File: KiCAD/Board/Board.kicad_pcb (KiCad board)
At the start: 2 copper layers, 84 parts, among them J1 MOTOR_5PIN_CONNECTOR, J2 DELAY_2PIN_CONNECTOR, J3 BATTERY_2PIN_CONNECTOR, Q1 AO3400A, Q2 AO3400A, Q3 AO3400A, Q4 AO3400A, Q5 SFH309, Q6 SFH309, U1 4040, U2 7421, U3 74LS393, U4 74HC164, U5 NE556, U6 ULN2003, U7 ULN2003, U8 LM7805_TO220

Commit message: Updated On May 29th 2025
KiCAD Board Almost Done. Will require minor touch ups tomm.
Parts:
- removed J2: DELAY_2PIN_CONNECTOR, Connector_PinSocket_2.54mm:PinSocket_1x02_P2.54mm_Vertical
- removed R6: R4.7K, Resistor_SMD:R_1210_3225Metric
- added C1: C0.1uf, Capacitor_THT:C_Disc_D5.0mm_W2.5mm_P2.50mm, F.Cu at (122.2, 151.6)
- added C2: C0.1uf, Capacitor_THT:C_Disc_D5.0mm_W2.5mm_P2.50mm, F.Cu at (126.5, 132.8)
- added D14: LED, LED_THT:LED_D3.0mm, F.Cu at (117.6, 69.3)
- added D15: LED, LED_THT:LED_D3.0mm, F.Cu at (112.4, 69.2)
- added D16: LED, LED_THT:LED_D3.0mm, F.Cu at (107.4, 69.2)
- added D17: LED, LED_THT:LED_D3.0mm, F.Cu at (102.4, 69.2)
- added JP1: JMP, Library:Jumper, F.Cu at (78.0, 102.1)
- added JP10: JMP, Library:Jumper, F.Cu at (58.9, 112.3)
- added JP11: JMP, Library:Jumper, F.Cu at (58.9, 114.9)
- added JP12: JMP, Library:Jumper, F.Cu at (58.9, 117.5)
- added JP13: JMP, Library:Jumper, F.Cu at (56.6, 131.3)
- added JP14: JMP, Library:Jumper, F.Cu at (15.0, 95.4)
- added JP15: JMP, Library:Jumper, F.Cu at (60.7, 122.2)
- added JP16: JMP, Library:Jumper, F.Cu at (104.9, 161.7)
- added JP17: JMP, Library:Jumper, F.Cu at (104.9, 164.3)
- added JP18: JMP, Library:Jumper, F.Cu at (84.1, 162.8)
- added JP19: JMP, Library:Jumper, F.Cu at (94.7, 122.7)
- added JP2: JMP, Library:Jumper, F.Cu at (86.9, 89.4)
- added JP20: JMP, Library:Jumper, F.Cu at (66.7, 127.4)
- added JP21: JMP, Library:Jumper, F.Cu at (136.8, 118.7)
- added JP23: JMP, Library:Jumper, F.Cu at (14.9, 106.4)
- added JP3: JMP, Library:Jumper, F.Cu at (43.9, 72.4)
- added JP4: JMP, Library:Jumper, F.Cu at (112.0, 123.7)
- added JP5: JMP, Library:Jumper, F.Cu at (85.6, 74.2)
- added JP6: JMP, Library:Jumper, F.Cu at (106.6, 113.5)
- added JP7: JMP, Library:Jumper, F.Cu at (108.5, 57.7)
- added JP8: JMP, Library:Jumper, F.Cu at (25.4, 146.1)
- added JP9: JMP, Library:Jumper, F.Cu at (34.5, 128.8)
- added R1: R4.7K, Resistor_THT:R_Axial_DIN0207_L6.3mm_D2.5mm_P10.16mm_Horizontal, F.Cu at (75.1, 96.5)
- added R2: R4.7K, Resistor_THT:R_Axial_DIN0207_L6.3mm_D2.5mm_P10.16mm_Horizontal, F.Cu at (30.7, 125.2)
- added SMD_2_DIP1: ~, Library:SMD_2_DIP, F.Cu at (85.9, 109.1)
- added SMD_2_DIP2: ~, Library:SMD_2_DIP, F.Cu at (80.8, 120.4)
- added SMD_2_DIP3: ~, Library:SMD_2_DIP, F.Cu at (50.5, 148.8)
- added SMD_2_DIP4: ~, Library:SMD_2_DIP, F.Cu at (62.7, 156.2)
- added U9: NE555P, Package_DIP:DIP-8_W7.62mm, F.Cu at (114.3, 138.2)
- C10, C13, C15, C16, C19, C23, C3, C6, C8: footprint Capacitor_SMD:C_1210_3225Metric_Pad1.33x2.70mm_HandSolder -> Capacitor_THT:C_Radial_D6.3mm_H5.0mm_P2.50mm
- C11, C12, C14, C18, C20, C21, C4, C5, C7, C9: footprint Capacitor_SMD:C_1210_3225Metric_Pad1.33x2.70mm_HandSolder -> Capacitor_THT:C_Disc_D5.0mm_W2.5mm_P2.50mm
- C17: value C0.1uf -> C10uf; footprint Capacitor_SMD:C_1210_3225Metric_Pad1.33x2.70mm_HandSolder -> Capacitor_THT:C_Radial_D6.3mm_H5.0mm_P2.50mm
- D10, D11, D12, D3, D4, D5, D6, D7, D8, D9: footprint Diode_SMD:D_1210_3225Metric -> Diode_THT:D_DO-35_SOD27_P12.70mm_Horizontal
- D2: footprint LED_SMD:LED_1210_3225Metric -> LED_THT:LED_D3.0mm
- J1: footprint Connector_PinSocket_1.27mm:PinSocket_1x05_P1.27mm_Vertical -> Connector_PinSocket_2.54mm:PinSocket_1x05_P2.54mm_Vertical
- R10, R11, R12, R13, R14, R15, R16, R17, R18, R19, R20, R21, R22, R23, R24, R25, R26, R27, R28, R29, R3, R30, R31, R32, R4, R5, R7, R8, R9: footprint Resistor_SMD:R_1210_3225Metric -> Resistor_THT:R_Axial_DIN0207_L6.3mm_D2.5mm_P10.16mm_Horizontal
- U5: value NE556 -> NE555P; footprint Package_DIP:DIP-14_W7.62mm_Socket -> Package_DIP:DIP-8_W7.62mm
- moved R4 225.8 mm to (109.5, 117.3), turned to -90 degrees
- moved R28 223.6 mm to (139.7, 86.4), turned to -90 degrees
- moved R13 223.6 mm to (127.4, 75.1), turned to 90 degrees
- moved U3 223.4 mm to (123.7, 78.0)
- moved R27 220.3 mm to (135.1, 86.6), turned to -90 degrees
- moved R21 219.7 mm to (104.4, 143.3), turned to -90 degrees
- moved R14 216.1 mm to (119.3, 83.1), turned to 90 degrees
- moved R26 214.1 mm to (109.5, 143.3), turned to -90 degrees
- moved R15 208.2 mm to (114.8, 72.9), turned to -90 degrees
- moved R16 206.6 mm to (110.4, 88.1), turned to 90 degrees
- moved U2 203.7 mm to (90.7, 79.2)
- moved R17 201.8 mm to (105.9, 90.7), turned to 90 degrees
- moved R3 198.7 mm to (86.5, 97.7)
- moved R11 198.2 mm to (93.3, 101.0), turned to 180 degrees
- moved C20 196.7 mm to (137.7, 83.1), turned to 180 degrees
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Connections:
- net Net-(R7-Pad1) renamed /7421_P2
- net Net-(R8-Pad1) renamed /7421_P4
- C12 pad 1: +5V -> Net-(JP21-A)
- C13 pad 1: +5V -> Net-(JP21-A)
- C14 pad 2: Net-(U5A-CV) -> Net-(U5-CV)
- C17 pad 1: GND -> Net-(JP21-A)
- C17 pad 2: Net-(U5B-CV) -> GND
- C18 pad 1: +5V -> /ADHOC_LED_5V
- C19 pad 1: +5V -> /ADHOC_LED_5V
- C22 pad 1: Net-(J2-Pin_1) -> Net-(JP8-B)
- D11 pad 1: /MOTOR_RESET -> Net-(D11-K)
- D12 pad 1: /MOTOR_RESET -> Net-(D12-K)
- D2 pad 1: GND -> Net-(D2-K)
- D2 pad 2: Net-(D2-A) -> /ADHOC_LED_5V
- D4 pad 1: Net-(D10-K) -> Net-(D4-K)
- D5 pad 1: Net-(D10-K) -> Net-(D4-K)
- D6 pad 1: Net-(D10-K) -> Net-(D4-K)
- D7 pad 1: Net-(D10-K) -> Net-(D4-K)
- D8 pad 1: Net-(D10-K) -> Net-(D4-K)
- J1 pad 1: +5V -> Net-(J1-Pin_1)
- Q2 pad 2: Net-(Q2-S) -> GND
- Q2 pad 3: GND -> Net-(Q2-D)
- Q3 pad 2: Net-(Q3-S) -> GND
- Q3 pad 3: GND -> Net-(Q3-D)
- Q4 pad 2: unconnected-(Q4-S-Pad2) -> GND
- Q4 pad 3: GND -> Net-(D12-A)
- R10 pad 1: Net-(R10-Pad1) -> /7421_P1
- R18 pad 1: +5V -> Net-(JP21-A)
- R20 pad 1: +5V -> /ADHOC_LED_5V
- R20 pad 2: Net-(U4-DSA) -> Net-(U4-~{MR})
- R21 pad 1: /MOTOR_CLOCK -> Net-(U9-Q)
- R21 pad 2: Net-(U4-CP) -> Net-(JP16-A)
- R26 pad 1: /MOTOR_CLOCK -> Net-(U9-Q)
- R26 pad 2: Net-(U3B-CP) -> Net-(JP17-A)
- R28 pad 1: /LOAD -> Net-(U3B-Q1)
- R28 pad 2: Net-(U4-DSB) -> Net-(JP9-B)
- R29 pad 1: /REVERSE_MOTION -> Net-(JP19-A)
- R31 pad 1: +5V -> /ADHOC_LED_5V
- R32 pad 2: /REVERSE_MOTION -> Net-(JP18-B)
- R4 pad 1: /SYSTEM_CLOCK -> Net-(U5-Q)
- R4 pad 2: Net-(U1-CLK) -> Net-(JP3-A)
- R5 pad 1: Net-(U1-Q0) -> Net-(D3-A)
- R5 pad 2: Net-(D2-A) -> Net-(D2-K)
- R9 pad 1: Net-(R9-Pad1) -> /7421_P5
- RV1 pad 3: +5V -> Net-(JP21-A)
- RV3 pad 1: Net-(J2-Pin_1) -> unconnected-(RV3-Pad1)
- RV3 pad 2: Net-(Q4-G) -> Net-(JP8-B)
- RV3 pad 3: unconnected-(RV3-Pad3) -> Net-(Q4-G)
- U1 pad 10: Net-(U1-CLK) -> /SYSTEM_CLOCK
- U1 pad 9: Net-(U1-Q0) -> Net-(D3-A)
- U2 pad 1: Net-(R10-Pad1) -> Net-(JP5-B)
- U2 pad 5: Net-(R9-Pad1) -> Net-(JP2-B)
- U3 pad 10: /LOAD -> Net-(U3B-Q1)
- U3 pad 13: Net-(U3B-CP) -> /MOTOR_CLOCKB
- U4 pad 14: +5V -> /ADHOC_LED_5V
- U4 pad 2: Net-(U4-DSB) -> /LOAD
- U4 pad 8: Net-(U4-CP) -> /MOTOR_CLOCKA
- U4 pad 9: Net-(U4-DSA) -> Net-(U4-~{MR})
- U5 pad 1: /DIS_SYS -> GND
- U5 pad 3: Net-(U5A-CV) -> Net-(U5-Q)
- U5 pad 4: +5V -> Net-(JP4-B)
- U5 pad 5: /SYSTEM_CLOCK -> Net-(U5-CV)
- U5 pad 7: GND -> /DIS_SYS
- U5 pad 8: /TRIG_MOTOR -> Net-(JP21-A)
- U6 pad 8: Net-(Q3-S) -> Net-(Q3-D)
- U7 pad 1: /S0 -> unconnected-(U7-I1-Pad1)
- U7 pad 10: unconnected-(U7-O7-Pad10) -> /MOTOR1
- U7 pad 11: unconnected-(U7-O6-Pad11) -> /MOTOR2
- U7 pad 12: unconnected-(U7-O5-Pad12) -> /MOTOR3
- U7 pad 13: /MOTOR1 -> /MOTOR4
- U7 pad 14: /MOTOR2 -> unconnected-(U7-O3-Pad14)
- U7 pad 15: /MOTOR3 -> unconnected-(U7-O2-Pad15)
- U7 pad 16: /MOTOR4 -> unconnected-(U7-O1-Pad16)
- U7 pad 2: /S1 -> unconnected-(U7-I2-Pad2)
- U7 pad 3: /S2 -> unconnected-(U7-I3-Pad3)
- U7 pad 4: /S3 -> Net-(JP13-A)
- U7 pad 5: unconnected-(U7-I5-Pad5) -> Net-(JP12-A)
- U7 pad 6: unconnected-(U7-I6-Pad6) -> Net-(JP11-A)
- U7 pad 7: unconnected-(U7-I7-Pad7) -> Net-(JP10-A)
- U7 pad 8: Net-(Q2-S) -> Net-(Q2-D)
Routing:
- net GND: track 28.8 -> 665.5 mm
- net +5V: track 19.9 -> 119.2 mm
- net /ADHOC_LED_5V: track 0.00 -> 97.8 mm
- net Net-(JP21-A): track 0.00 -> 82.5 mm
- net Net-(Q1-D): track 0.00 -> 49.3 mm
- net Net-(D14-A): track 0.00 -> 33.9 mm
- net Net-(D10-K): track 0.00 -> 30.2 mm
- net Net-(D15-A): track 0.00 -> 29.3 mm
- net Net-(D14-K): track 0.00 -> 27.3 mm
- net Net-(Q4-G): track 0.00 -> 26.7 mm
- net Net-(D4-K): track 0.00 -> 24.8 mm
- net /TRIG_MOTOR: track 9.57 -> 34.2 mm
- net Net-(D16-A): track 0.00 -> 23.6 mm
- net /7421_P4: track 0.00 -> 22.6 mm
- net Net-(D12-A): track 0.00 -> 22.1 mm
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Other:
- board outline added: 122.9 x 109.7 mm

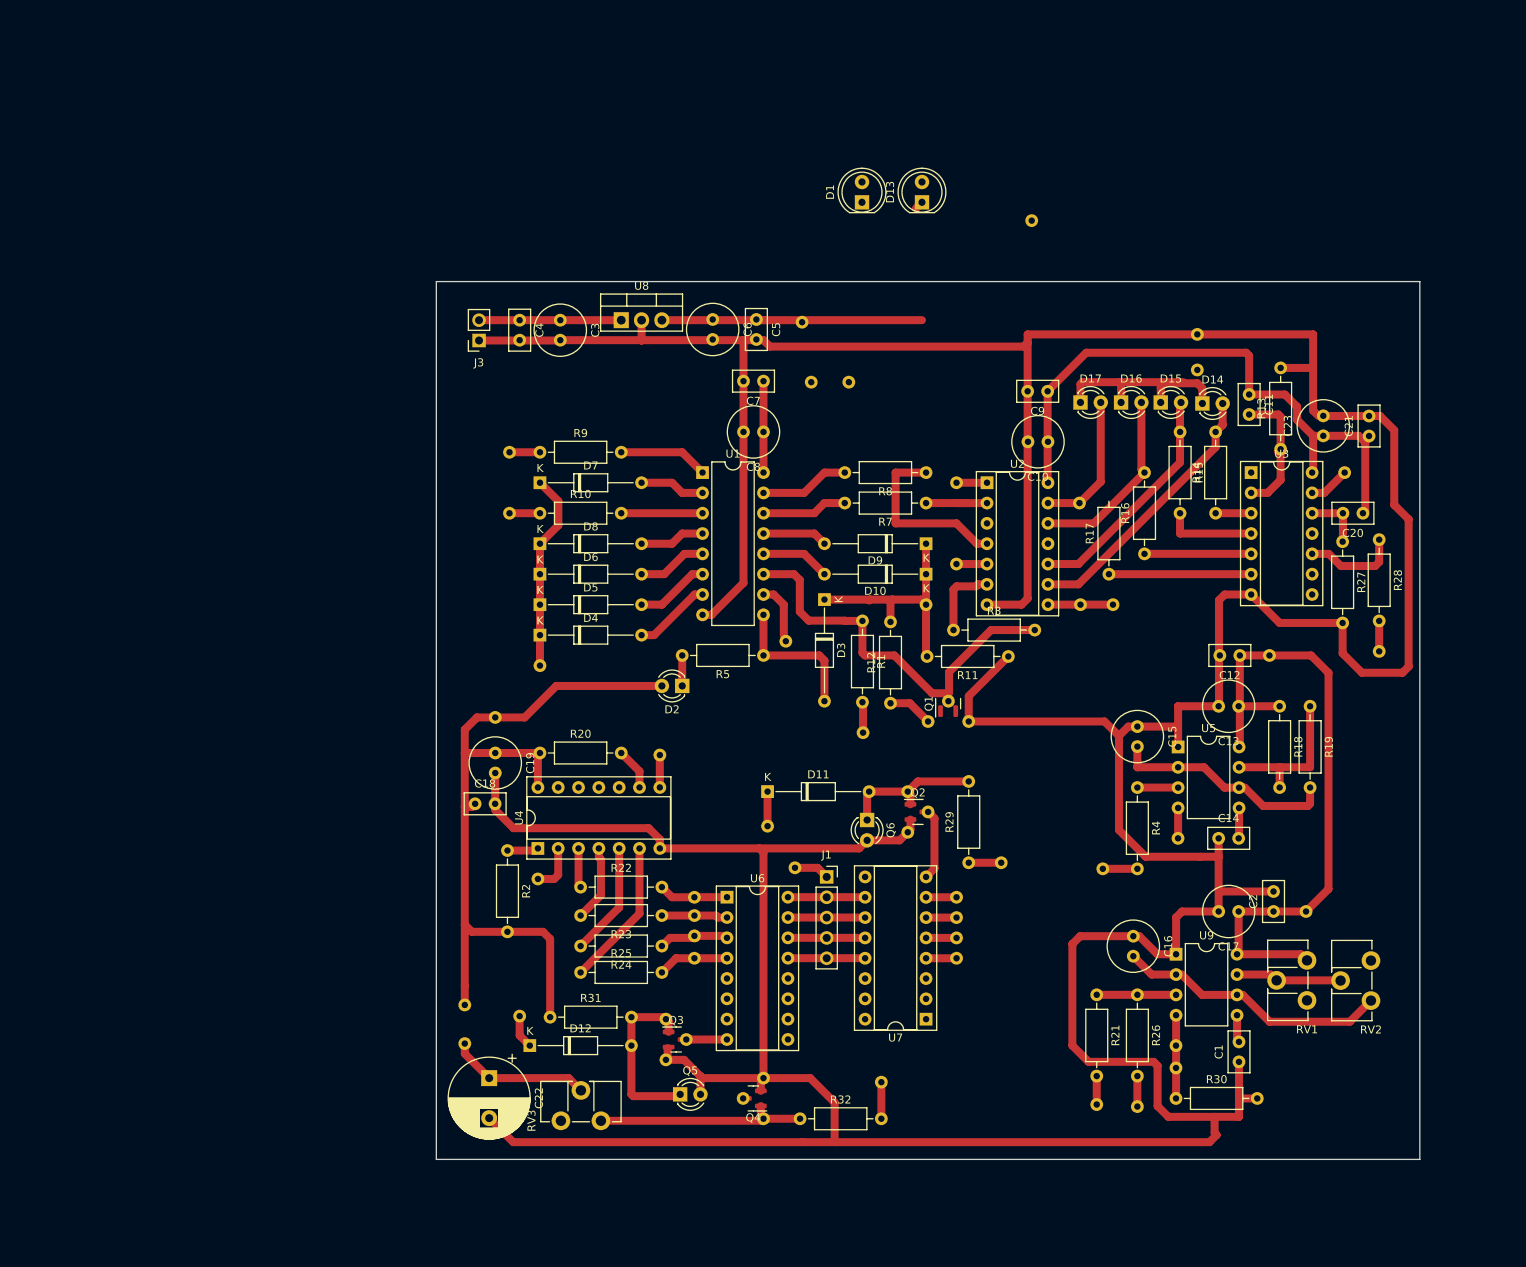
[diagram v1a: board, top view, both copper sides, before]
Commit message: May 31st 2025 Updated
Major Design Changed. using LM393 instead of 74HC21 to get half an hour clock signal into hour counter.
connections are more streamlined and easy to solder. Less components as well. went down from 5 mosfets to now just 2 and chips are 6 in total
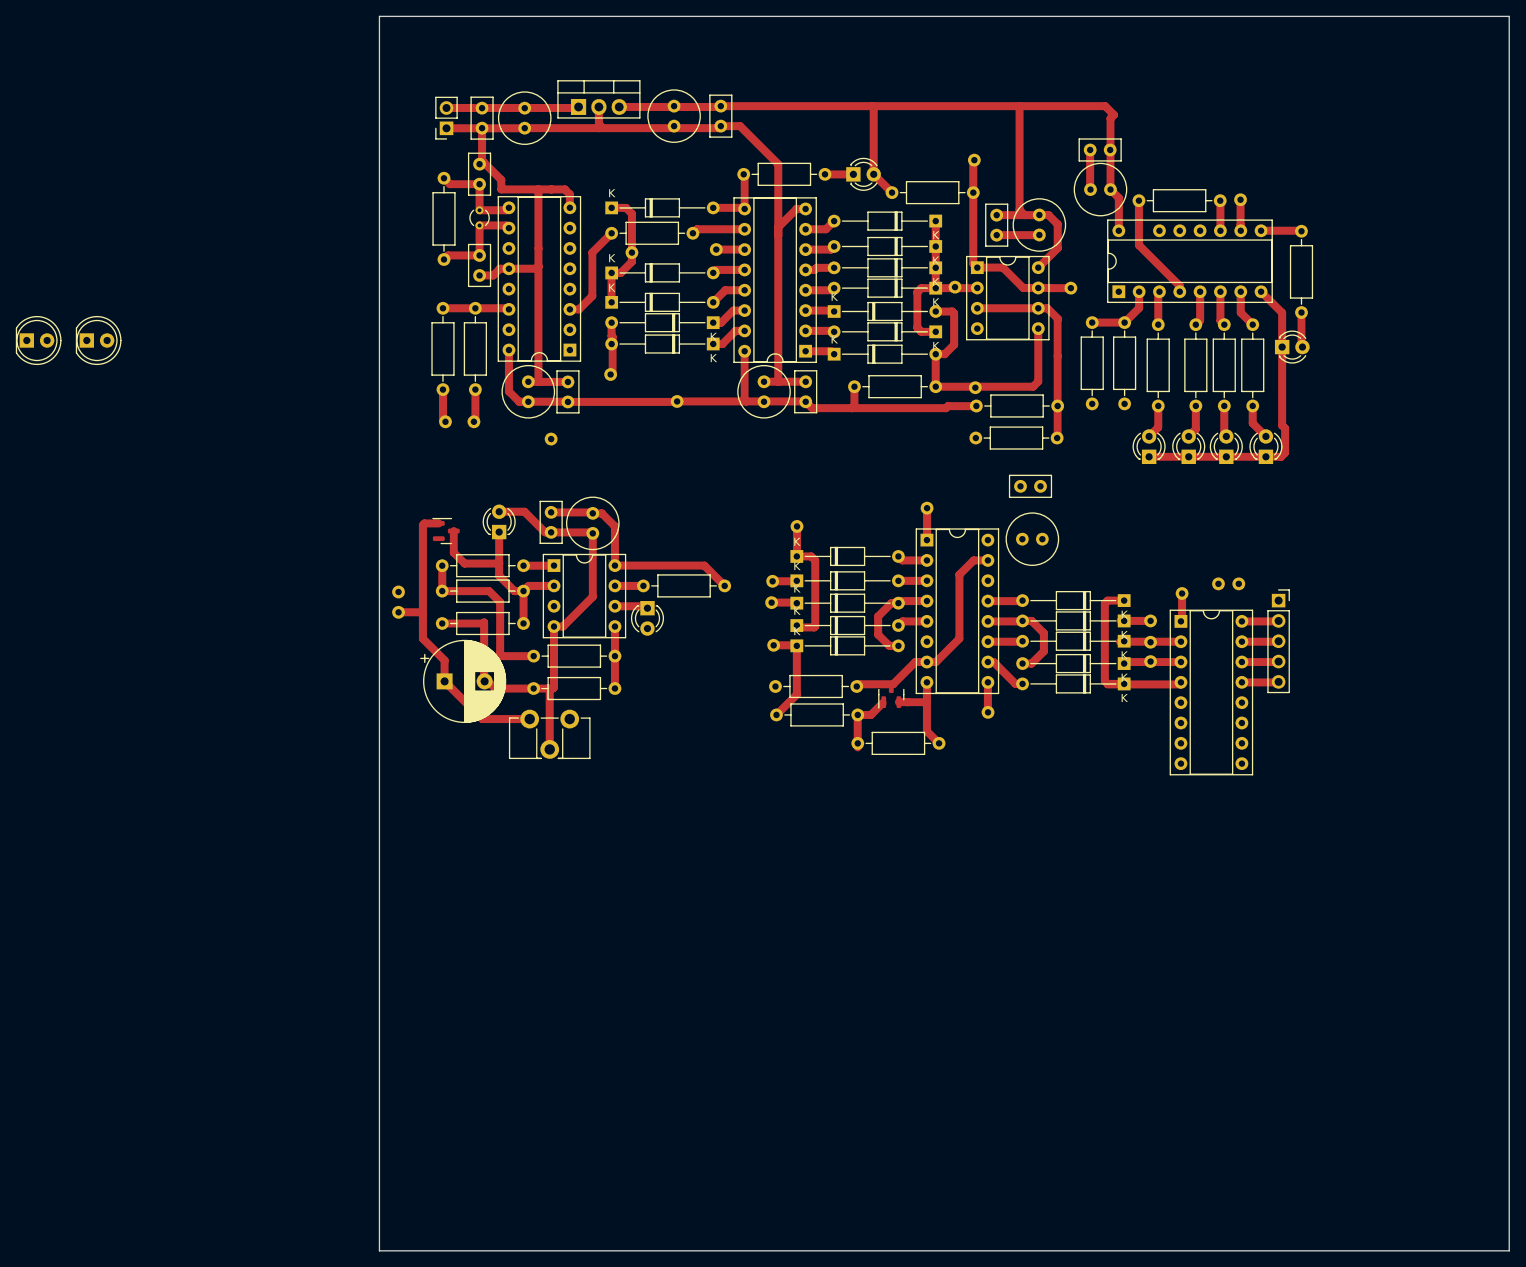
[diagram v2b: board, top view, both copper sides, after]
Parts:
- removed C16, C17, C19, C23: C10uf, Capacitor_THT:C_Radial_D6.3mm_H5.0mm_P2.50mm
- removed C18, C20, C21: C0.1uf, Capacitor_THT:C_Disc_D5.0mm_W2.5mm_P2.50mm
- removed C22: C100uf, Capacitor_THT:CP_Radial_D10.0mm_P5.00mm
- removed D11, D12: D4148, Diode_THT:D_DO-35_SOD27_P12.70mm_Horizontal
- removed D16: LED, LED_THT:LED_D3.0mm
- removed JP13, JP14, JP15, JP16, JP17, JP18, JP19, JP21, JP23: JMP, Library:Jumper
- removed Q2, Q3, Q4: AO3400A, Package_TO_SOT_SMD:SOT-23
- removed Q6: SFH309, LED_THT:LED_D3.0mm_Clear
- removed R2, R20, R22, R23, R24, R25, R29, R31, R32: R4.7K, Resistor_THT:R_Axial_DIN0207_L6.3mm_D2.5mm_P10.16mm_Horizontal
- removed RV2, RV3: POT100K, Potentiometer_THT:Potentiometer_ACP_CA9-H3,8_Horizontal
- removed SMD_2_DIP1, SMD_2_DIP2, SMD_2_DIP3, SMD_2_DIP4: ~, Library:SMD_2_DIP
- removed U4: 74HC164, Package_DIP:DIP-14_W7.62mm_Socket
- removed U6, U7: ULN2003, Package_DIP:DIP-16_W7.62mm_Socket
- added C24: C22pF, Capacitor_THT:C_Disc_D5.0mm_W2.5mm_P2.50mm, F.Cu at (27.2, 50.8)
- added C25: C22pF, Capacitor_THT:C_Disc_D5.0mm_W2.5mm_P2.50mm, F.Cu at (27.2, 41.9)
- added C26: C0.1uf, Capacitor_THT:C_Disc_D5.0mm_W2.5mm_P2.50mm, F.Cu at (38.3, 69.1)
- added C27: C10uf, Capacitor_THT:C_Radial_D6.3mm_H5.0mm_P2.50mm, F.Cu at (33.3, 69.1)
- added D18: D4148, Diode_THT:D_DO-35_SOD27_P12.70mm_Horizontal, F.Cu at (71.6, 63.2)
- added D19: D4148, Diode_THT:D_DO-35_SOD27_P12.70mm_Horizontal, F.Cu at (56.5, 61.9)
- added D20: D4148, Diode_THT:D_DO-35_SOD27_P12.70mm_Horizontal, F.Cu at (56.5, 59.2)
- added D21: D4148, Diode_THT:D_DO-35_SOD27_P12.70mm_Horizontal, F.Cu at (71.6, 57.8)
- added D22: LED, LED_THT:LED_D3.0mm, F.Cu at (127.6, 62.3)
- added D23: LED, LED_THT:LED_D3.0mm, F.Cu at (125.5, 76.0)
- added D24: LED, LED_THT:LED_D3.0mm, F.Cu at (120.6, 76.0)
- added D25: LED, LED_THT:LED_D3.0mm, F.Cu at (115.9, 76.0)
- added D26: LED, LED_THT:LED_D3.0mm, F.Cu at (110.9, 76.0)
- added D27: D4148, Diode_THT:D_DO-35_SOD27_P12.70mm_Horizontal, F.Cu at (107.8, 104.4)
- added D28: D4148, Diode_THT:D_DO-35_SOD27_P12.70mm_Horizontal, F.Cu at (107.8, 94.0)
- added D29: D4148, Diode_THT:D_DO-35_SOD27_P12.70mm_Horizontal, F.Cu at (107.8, 99.1)
- added D30: D4148, Diode_THT:D_DO-35_SOD27_P12.70mm_Horizontal, F.Cu at (66.9, 88.5)
- added D31: D4148, Diode_THT:D_DO-35_SOD27_P12.70mm_Horizontal, F.Cu at (107.8, 101.9)
- added D32: D4148, Diode_THT:D_DO-35_SOD27_P12.70mm_Horizontal, F.Cu at (107.8, 96.5)
- added D33: D4148, Diode_THT:D_DO-35_SOD27_P12.70mm_Horizontal, F.Cu at (66.9, 94.3)
- added Q7: AO3400A, Package_TO_SOT_SMD:SOT-23, F.Cu at (23.1, 85.3)
- added Q8: SFH309, LED_THT:LED_D3.0mm_Clear, F.Cu at (48.2, 94.9)
- added R33: R4.7K, Resistor_THT:R_Axial_DIN0207_L6.3mm_D2.5mm_P10.16mm_Horizontal, F.Cu at (53.9, 48.1)
- added R34: R4.7K, Resistor_THT:R_Axial_DIN0207_L6.3mm_D2.5mm_P10.16mm_Horizontal, F.Cu at (107.9, 59.2)
- added R35: R4.7K, Resistor_THT:R_Axial_DIN0207_L6.3mm_D2.5mm_P10.16mm_Horizontal, F.Cu at (103.8, 59.2)
- added R6: R1MEG, Resistor_THT:R_Axial_DIN0207_L6.3mm_D2.5mm_P10.16mm_Horizontal, F.Cu at (22.8, 51.3)
- added U10: ULN2003A, Package_DIP:DIP-16_W7.62mm_Socket, F.Cu at (114.9, 96.6)
- added U11: CD4060BE, Package_DIP:DIP-16_W7.62mm_Socket, F.Cu at (38.5, 62.7)
- added Y1: Crystal, Crystal:Crystal_DS26_D2.0mm_L6.0mm_Vertical, F.Cu at (27.2, 45.2)
- C12, C14, C2: value C0.1uf -> C10uf; footprint Capacitor_THT:C_Disc_D5.0mm_W2.5mm_P2.50mm -> Capacitor_THT:C_Radial_D6.3mm_H5.0mm_P2.50mm
- C13: value C10uf -> C0.1uf; footprint Capacitor_THT:C_Radial_D6.3mm_H5.0mm_P2.50mm -> Capacitor_THT:C_Disc_D5.0mm_W2.5mm_P2.50mm
- C15: value C10uf -> C100uF; footprint Capacitor_THT:C_Radial_D6.3mm_H5.0mm_P2.50mm -> Capacitor_THT:CP_Radial_D10.0mm_P5.00mm
- D14, D15, D17: value LED -> D4148; footprint LED_THT:LED_D3.0mm -> Diode_THT:D_DO-35_SOD27_P12.70mm_Horizontal
- R11, R27, R30: value R10K -> R4.7K
- R13: value R10K -> R47K
- R18: value R8.2K -> R4.7K
- R19: value R68K -> R4.7K
- U1: footprint Package_DIP:DIP-16_W7.62mm -> Package_DIP:DIP-16_W7.62mm_Socket
- U2: value 7421 -> 4015; footprint Package_DIP:DIP-14_W7.62mm_Socket -> Package_DIP:DIP-16_W7.62mm_Socket
- U3: value 74LS393 -> LM393; footprint Package_DIP:DIP-14_W7.62mm_Socket -> Package_DIP:DIP-8_W7.62mm_Socket
- U5: value NE555P -> 4040; footprint Package_DIP:DIP-8_W7.62mm -> Package_DIP:DIP-16_W7.62mm_Socket
- U9: value NE555P -> LM393; footprint Package_DIP:DIP-8_W7.62mm -> Package_DIP:DIP-8_W7.62mm_Socket
- moved C1 115.1 mm to (106.1, 37.7), turned to 180 degrees
- moved R27 113.0 mm to (22.6, 96.8), turned to 0 degrees
- moved R28 106.7 mm to (34.0, 100.9), turned to 0 degrees
- moved D1 105.8 mm to (-29.3, 61.5), turned to 0 degrees
- moved D13 105.8 mm to (-21.8, 61.5), turned to 0 degrees
- moved R26 100.5 mm to (22.6, 92.8), turned to 0 degrees
- moved R21 99.4 mm to (109.7, 44.0), turned to 0 degrees
- moved RV1 98.6 mm to (38.5, 108.8), turned to -90 degrees
- moved R30 95.2 mm to (34.0, 105.0)
- moved R16 92.9 mm to (22.7, 57.4), turned to -90 degrees
- moved C2 92.5 mm to (106.1, 42.6), turned to 180 degrees
- moved R10 90.1 mm to (123.9, 69.7), turned to 90 degrees
- moved R15 89.4 mm to (26.7, 57.4)
- moved U9 89.3 mm to (89.5, 52.4)
- moved C13 89.3 mm to (36.2, 83.0), turned to -90 degrees
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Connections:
- net Net-(D10-A) renamed /Q8
- net Net-(D3-A) renamed /Q0
- net Net-(D9-A) renamed /Q7
- C1 pad 1: GND -> +5V
- C1 pad 2: Net-(U9-CV) -> GND
- C11 pad 2: Net-(U3A-MR) -> GND
- C12 pad 1: Net-(JP21-A) -> +5V
- C13 pad 1: Net-(JP21-A) -> +5V
- C14 pad 1: GND -> +5V
- C14 pad 2: Net-(U5-CV) -> GND
- C15 pad 1: GND -> Net-(JP1-B)
- C15 pad 2: /TRIG_SYS -> GND
- C2 pad 1: Net-(JP21-A) -> +5V
- C7 pad 1: +5V -> Net-(JP6-A)
- C8 pad 1: +5V -> Net-(JP6-A)
- D14 pad 1: Net-(D14-K) -> /F1
- D15 pad 1: Net-(D14-K) -> Net-(D15-K)
- D17 pad 1: Net-(D14-K) -> Net-(D17-K)
- D2 pad 2: /ADHOC_LED_5V -> +5V
- JP1 pad 1: Net-(D4-K) -> +5V
- JP1 pad 2: Net-(D10-K) -> Net-(JP1-B)
- JP10 pad 2: /S3 -> Net-(D15-K)
- JP11 pad 2: /S2 -> /MOTOR_CLOCK_A
- JP12 pad 2: /S1 -> /MOTOR_CLOCK_B
- JP2 pad 1: /7421_P5 -> Net-(JP2-A)
- JP3 pad 1: Net-(JP3-A) -> Net-(D18-A)
- JP3 pad 2: /SYSTEM_CLOCK -> Net-(D19-A)
- JP4 pad 1: Net-(JP21-A) -> Net-(D10-K)
- JP4 pad 2: Net-(JP4-B) -> Net-(D4-K)
- JP5 pad 1: /7421_P1 -> Net-(JP2-A)
- JP7 pad 1: Net-(D14-K) -> /F1
- JP7 pad 2: GND -> Net-(JP7-B)
- JP8 pad 1: /ADHOC_LED_5V -> Net-(D33-K)
- JP8 pad 2: Net-(JP8-B) -> /F2
- JP9 pad 1: /LOAD -> Net-(D17-K)
- JP9 pad 2: Net-(JP9-B) -> /F3
- Q5 pad 1: Net-(D12-A) -> Net-(Q5-C)
- R1 pad 1: Net-(Q1-D) -> Net-(D15-K)
- R1 pad 2: Net-(JP6-A) -> Net-(Q1-G)
- R10 pad 1: /7421_P1 -> Net-(D23-A)
- R10 pad 2: Net-(U1-Q4) -> Net-(U5-Q1)
- R11 pad 1: GND -> Net-(D24-A)
- R11 pad 2: Net-(D10-K) -> Net-(U5-Q2)
- R12 pad 1: Net-(Q1-G) -> Net-(D25-A)
- R12 pad 2: Net-(D10-K) -> Net-(U5-Q3)
- R13 pad 1: Net-(U3A-MR) -> GND
- R13 pad 2: GND -> Net-(Q1-G)
- R14 pad 1: Net-(U3A-Q0) -> Net-(Q1-D)
- R14 pad 2: Net-(D14-A) -> +5V
- R15 pad 1: Net-(D15-A) -> Net-(U11-Q8)
- R15 pad 2: Net-(U3A-Q1) -> /MOTOR_CLOCK_A
- R16 pad 1: Net-(U3A-Q2) -> Net-(U11-Q8)
- R16 pad 2: Net-(D16-A) -> /MOTOR_CLOCK_B
- R17 pad 1: Net-(U3A-Q3) -> +5V
- R17 pad 2: Net-(D17-A) -> /F_RESET
- R18 pad 1: Net-(JP21-A) -> Net-(D26-A)
- R18 pad 2: /DIS_SYS -> Net-(U5-Q4)
- R19 pad 1: /DIS_SYS -> +5V
- R19 pad 2: /TRIG_SYS -> /R_RESET
- R21 pad 1: Net-(U9-Q) -> Net-(U5-Q6)
- R21 pad 2: Net-(JP16-A) -> Net-(U5-Reset)
- R26 pad 1: Net-(U9-Q) -> +5V
- R26 pad 2: Net-(JP17-A) -> Net-(Q5-C)
- R27 pad 1: Net-(U3B-MR) -> GND
- R27 pad 2: GND -> Net-(Q5-C)
- R28 pad 1: Net-(U3B-Q1) -> +5V
- R28 pad 2: Net-(JP9-B) -> Net-(U3B-+)
- R3 pad 1: Net-(R3-Pad1) -> Net-(U5-Q0)
- R3 pad 2: Net-(Q1-D) -> Net-(D22-A)
- R30 pad 1: /MOTOR_RESET -> GND
- R30 pad 2: GND -> Net-(U3B-+)
- R4 pad 1: Net-(U5-Q) -> Net-(JP6-A)
- R4 pad 2: Net-(JP3-A) -> /REF2.5
- R7 pad 1: /7421_P2 -> GND
- R7 pad 2: Net-(U1-Q9) -> /REF2.5
- R8 pad 1: /7421_P4 -> Net-(D18-A)
- R8 pad 2: Net-(U1-Q10) -> Net-(JP6-A)
- R9 pad 1: /7421_P5 -> Net-(JP2-A)
- R9 pad 2: Net-(U1-Q11) -> +5V
- RV1 pad 2: /DIS_MOTOR -> GND
- RV1 pad 3: Net-(JP21-A) -> Net-(JP1-B)
- U1 pad 1: Net-(U1-Q11) -> Net-(D18-K)
- U1 pad 10: /SYSTEM_CLOCK -> Net-(U1-CLK)
- U1 pad 11: Net-(Q1-D) -> Net-(JP2-B)
- U1 pad 14: Net-(U1-Q9) -> Net-(D20-K)
- U1 pad 15: Net-(U1-Q10) -> Net-(D19-K)
- U1 pad 16: +5V -> Net-(JP6-A)
- U1 pad 3: Net-(U1-Q4) -> Net-(D21-K)
- U2 pad 1: Net-(JP5-B) -> Net-(JP12-A)
- U2 pad 10: Net-(D15-A) -> Net-(D27-A)
- U2 pad 11: (no net) -> Net-(D29-A)
- U2 pad 12: Net-(D16-A) -> Net-(D31-A)
- U2 pad 13: Net-(D17-A) -> Net-(D28-A)
- U2 pad 14: +5V -> /R_RESET
- U2 pad 2: /7421_P2 -> Net-(D30-A)
- U2 pad 3: (no net) -> Net-(D17-A)
- U2 pad 4: /7421_P4 -> Net-(D15-A)
- U2 pad 5: Net-(JP2-B) -> Net-(D14-A)
- U2 pad 6: Net-(R3-Pad1) -> /F_RESET
- U2 pad 7: GND -> Net-(Q1-D)
- U2 pad 8: /REVERSE_MOTION -> GND
- U2 pad 9: Net-(D14-A) -> Net-(JP11-A)
- U3 pad 1: Net-(Q1-D) -> /F_RESET
- U3 pad 2: Net-(U3A-MR) -> Net-(Q5-C)
- U3 pad 3: Net-(U3A-Q0) -> Net-(U3A-+)
- U3 pad 4: Net-(U3A-Q1) -> GND
- U3 pad 5: Net-(U3A-Q2) -> Net-(U3B-+)
- U3 pad 6: Net-(U3A-Q3) -> Net-(Q8-C)
- U3 pad 7: GND -> /R_RESET
- U3 pad 8: unconnected-(U3B-Q3-Pad8) -> +5V
- U5 pad 1: GND -> unconnected-(U5-Q11-Pad1)
- U5 pad 2: /TRIG_SYS -> /"R" CLOCK
- U5 pad 3: Net-(U5-Q) -> Net-(U5-Q4)
- U5 pad 4: Net-(JP4-B) -> Net-(U5-Q6)
- U5 pad 5: Net-(U5-CV) -> Net-(U5-Q3)
- U5 pad 6: /TRIG_SYS -> Net-(U5-Q2)
- U5 pad 7: /DIS_SYS -> Net-(U5-Q1)
- U5 pad 8: Net-(JP21-A) -> GND
- U9 pad 1: GND -> Net-(JP2-A)
- U9 pad 2: /TRIG_MOTOR -> Net-(D4-K)
- U9 pad 3: Net-(U9-Q) -> /REF2.5
- U9 pad 4: /MOTOR_RESET -> GND
- U9 pad 5: Net-(U9-CV) -> Net-(D18-A)
- U9 pad 6: /TRIG_MOTOR -> /REF2.5
- U9 pad 7: /DIS_MOTOR -> Net-(JP2-A)
- U9 pad 8: Net-(JP21-A) -> +5V
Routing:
- net GND: track 665.5 -> 265.9 mm
- net /ADHOC_LED_5V: track 97.8 -> 0.00 mm
- net Net-(JP21-A): track 82.5 -> 0.00 mm
- net Net-(JP6-A): track 3.84 -> 73.8 mm
- net +5V: track 119.2 -> 168.2 mm
- net Net-(JP1-B): track 0.00 -> 38.5 mm
- net /TRIG_MOTOR: track 34.2 -> 0.00 mm
- net Net-(D18-A): track 0.00 -> 32.9 mm
- net Net-(D14-A): track 33.9 -> 3.78 mm
- net /TRIG_SYS: track 28.4 -> 0.00 mm
- net Net-(D14-K): track 27.3 -> 0.00 mm
- net Net-(Q4-G): track 26.7 -> 0.00 mm
- net Net-(JP2-A): track 0.00 -> 26.5 mm
- net Net-(Q5-C): track 0.00 -> 26.4 mm
- net /REF2.5: track 0.00 -> 25.6 mm
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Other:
- board size 122.9 x 109.7 mm -> 141.2 x 154.3 mm
